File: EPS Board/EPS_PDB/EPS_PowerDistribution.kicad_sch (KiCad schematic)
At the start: 73 parts, among them U10 TPS259621DDAT, U11 LTC3624IDD-25PBF, U12 TPS259621DDAT, U13 TPS259621DDAT, U14 TPS259621DDAT, U15 TPS259621DDAT, U16 TPS259621DDAT, U17 LM5000-3MTCX, U18 AD7708BRUZ, U2 TS4061BICT-1.25, U6 TPS259621DDAT, U7 TPS259621DDAT, U9 TPS259621DDAT, Y4 32.768kHz

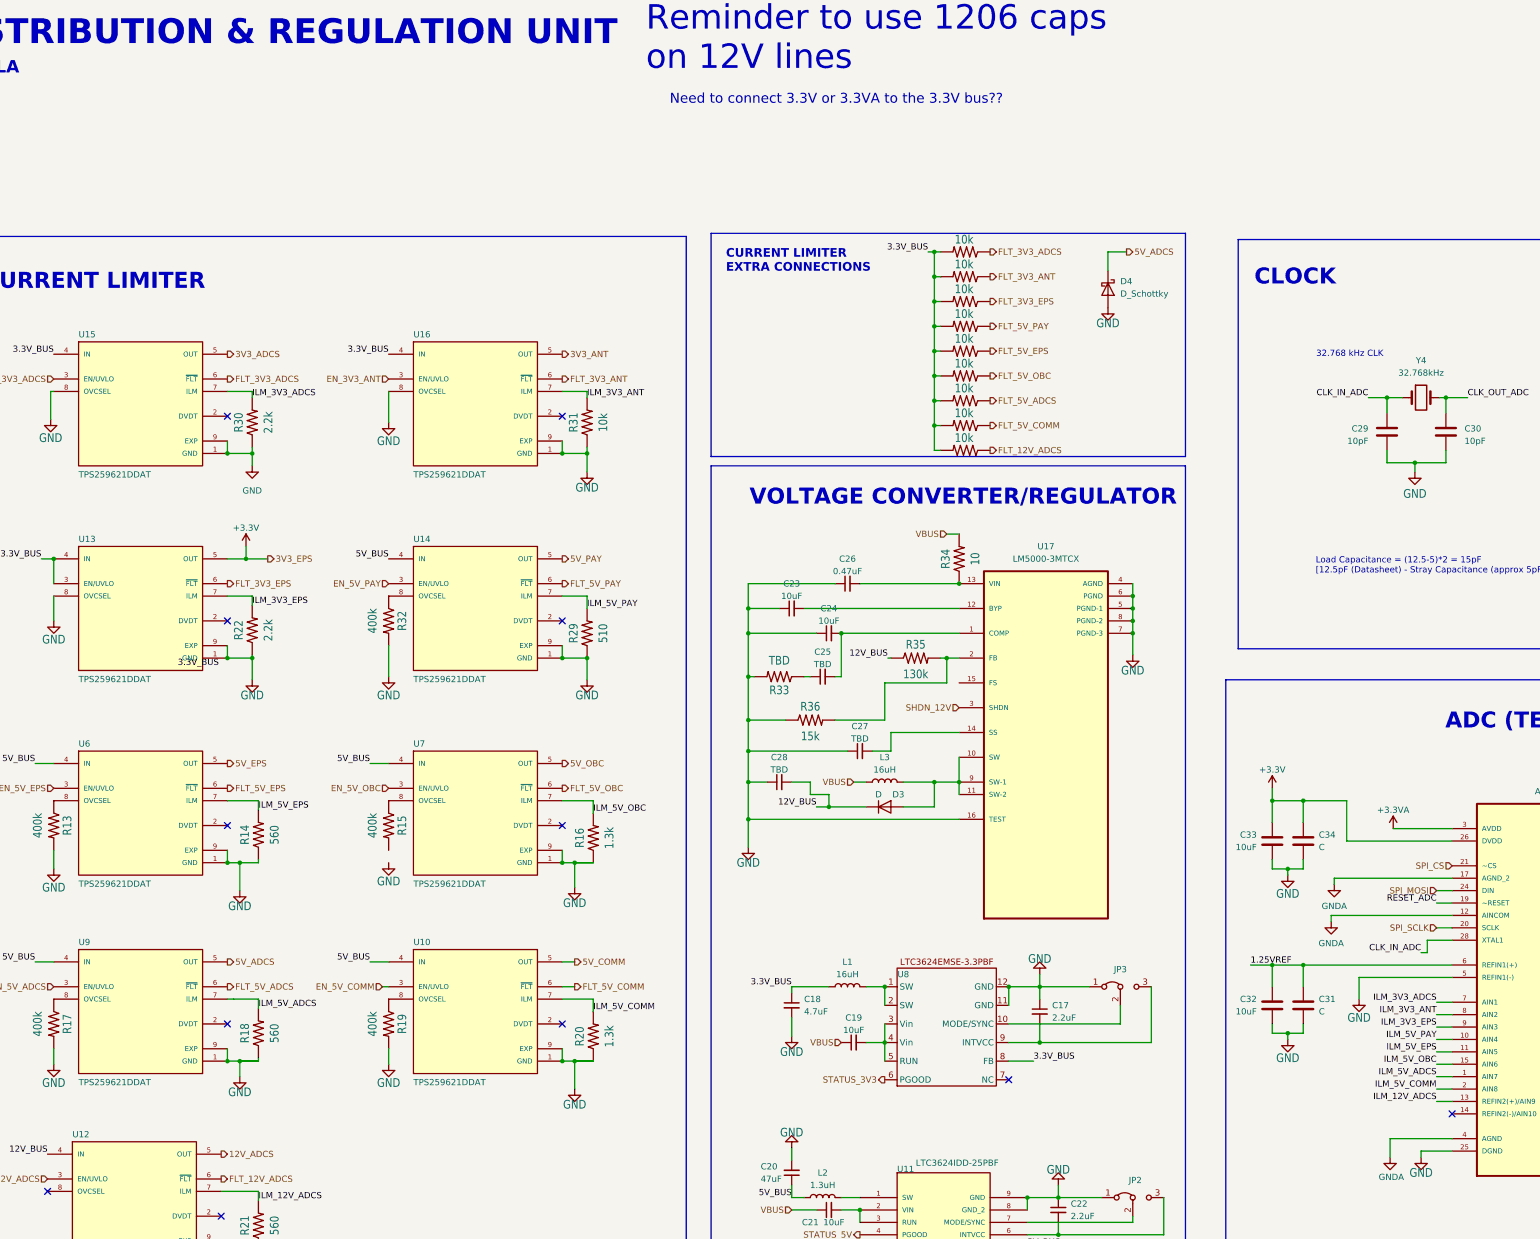
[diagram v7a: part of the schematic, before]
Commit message: texts added in schematics for clarity
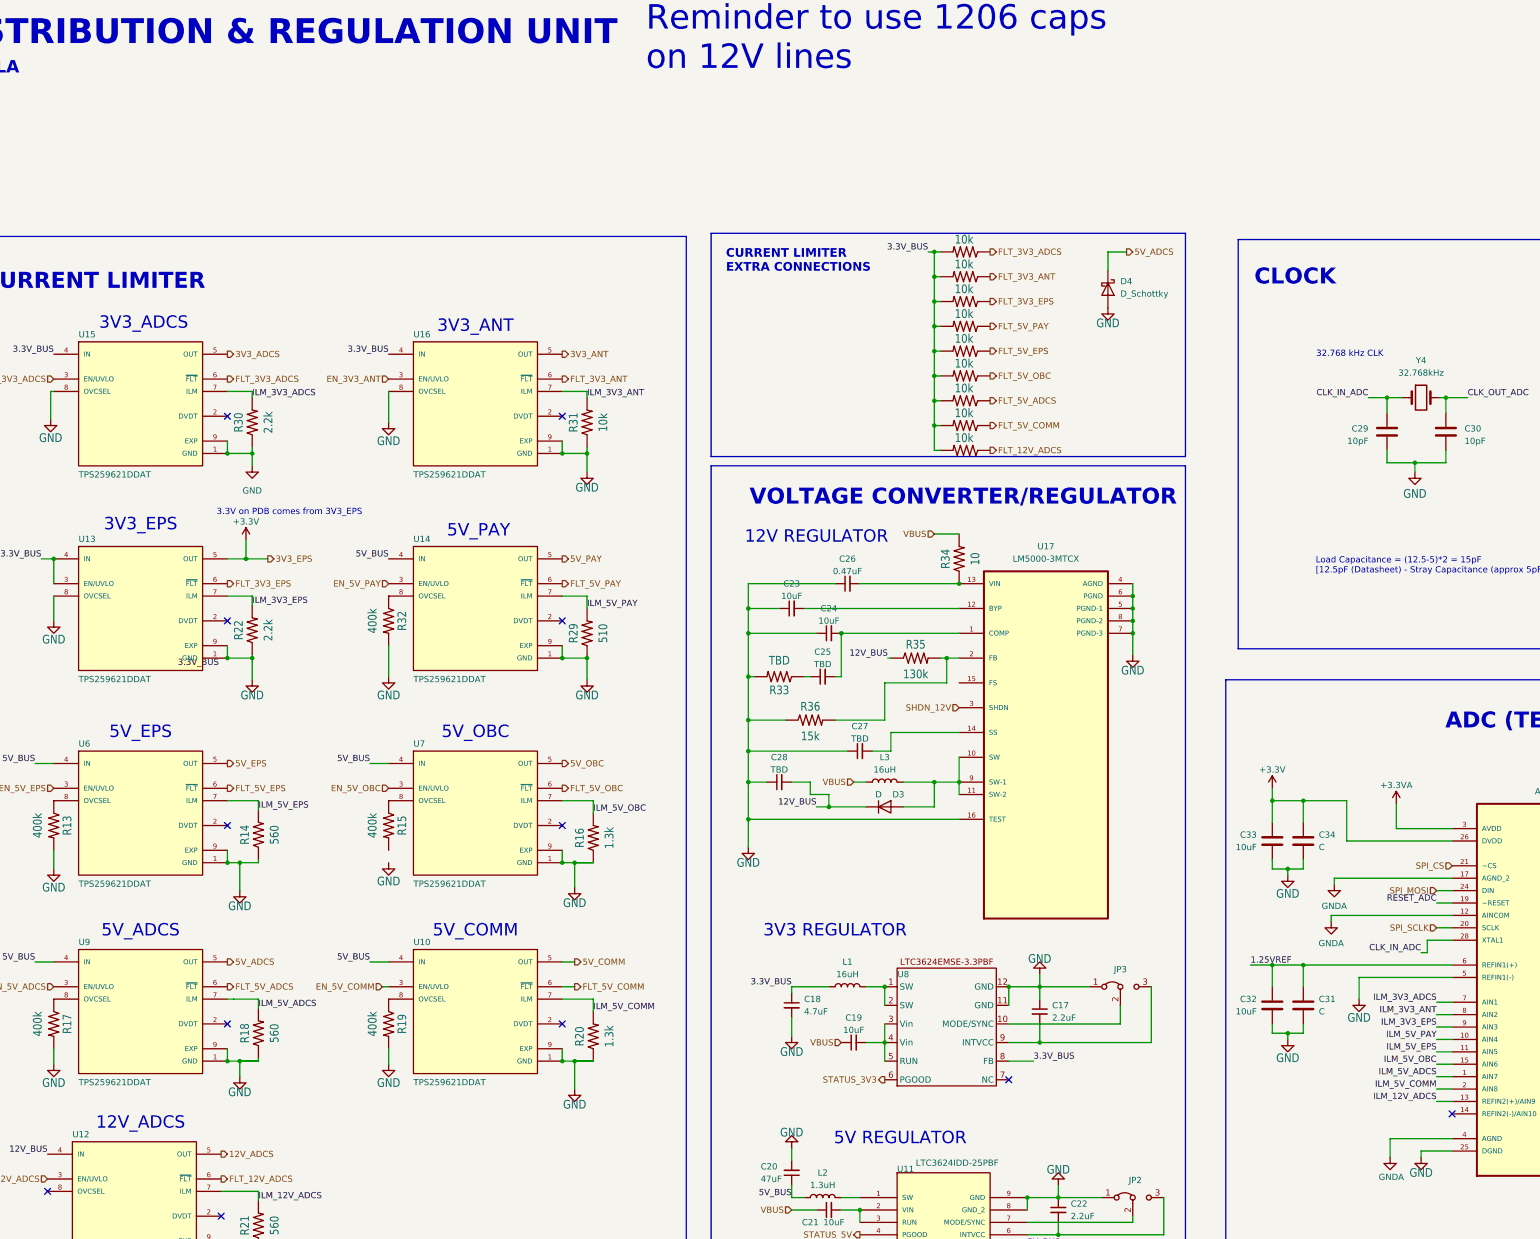
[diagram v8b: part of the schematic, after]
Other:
- note added: "12V REGULATOR"
- note added: "12V_ADCS"
- note added: "3.3V on PDB comes from 3V3_EPS"
- note added: "3V3 REGULATOR"
- note added: "3V3_ADCS"
- note added: "3V3_ANT"
- note added: "3V3_EPS"
- note added: "5V REGULATOR"
- note added: "5V_ADCS"
- note added: "5V_COMM"
- note added: "5V_EPS"
- note added: "5V_OBC"
- note added: "5V_PAY"
- note removed: "Need to connect 3.3V or 3.3VA to the 3.3V bus??"
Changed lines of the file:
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@@
 	(wire
 		(pts
-			(xy 334.01 186.69) (xy 346.075 186.69)
-		)
-		(stroke
-			(width 0)
-			(type default)
-		)
-	)
-	(wire
-		(pts
 			(xy 128.27 234.95) (xy 128.27 231.775)
 		)
@@
 	(wire
 		(pts
-			(xy 242.57 126.365) (xy 245.11 126.365)
+			(xy 240.03 126.365) (xy 245.11 126.365)
 		)
 		(stroke
@@
 	(wire
 		(pts
-			(xy 99.06 128.905) (xy 99.06 131.445)
+			(xy 99.06 127.635) (xy 99.06 131.445)
+		)
+		(stroke
+			(width 0)
+			(type default)
+		)
+	)
+	(wire
+		(pts
+			(xy 334.645 186.69) (xy 346.075 186.69)
 		)
 		(stroke
@@
 	(wire
 		(pts
+			(xy 334.645 181.61) (xy 334.645 186.69)
+		)
+		(stroke
+			(width 0)
+			(type default)
+		)
+	)
+	(wire
+		(pts
 			(xy 201.93 155.575) (xy 203.2 155.575)
 		)
@@
 		)
 	)
-	(text "Need to connect 3.3V or 3.3VA to the 3.3V bus??"
-		(exclude_from_sim no)
-		(at 219.964 37.338 0)
-		(effects
-			(font
-				(size 2.032 2.032)
-			)
-		)
-	)
 	(text "VOLTAGE CONVERTER/REGULATOR"
 		(exclude_from_sim no)
@@
 		)
 	)
+	(text "5V_EPS"
+		(exclude_from_sim no)
+		(at 77.47 167.005 0)
+		(effects
+			(font
+				(size 2.54 2.54)
+			)
+		)
+	)
 	(text "ADC (TELEMETRY)"
 		(exclude_from_sim no)
@@
 		)
 	)
+	(text "12V_ADCS"
+		(exclude_from_sim no)
+		(at 77.47 247.015 0)
+		(effects
+			(font
+				(size 2.54 2.54)
+			)
+		)
+	)
+	(text "5V_OBC"
+		(exclude_from_sim no)
+		(at 146.05 167.005 0)
+		(effects
+			(font
+				(size 2.54 2.54)
+			)
+		)
+	)
+	(text "12V REGULATOR"
+		(exclude_from_sim no)
+		(at 215.9 127 0)
+		(effects
+			(font
+				(size 2.54 2.54)
+			)
+		)
+	)
+	(text "5V_ADCS"
+		(exclude_from_sim no)
+		(at 77.47 207.645 0)
+		(effects
+			(font
+				(size 2.54 2.54)
+			)
+		)
+	)
+	(text "5V_COMM"
+		(exclude_from_sim no)
+		(at 146.05 207.645 0)
+		(effects
+			(font
+				(size 2.54 2.54)
+			)
+		)
+	)
+	(text "3V3_ANT"
+		(exclude_from_sim no)
+		(at 146.05 83.82 0)
+		(effects
+			(font
+				(size 2.54 2.54)
+			)
+		)
+	)
 	(text "CURRENT LIMITER \nEXTRA CONNECTIONS"
 		(exclude_from_sim no)
@@
 		)
 	)
+	(text "3.3V on PDB comes from 3V3_EPS"
+		(exclude_from_sim no)
+		(at 107.95 121.92 0)
+		(effects
+			(font
+				(size 1.27 1.27)
+			)
+		)
+	)
+	(text "3V3_EPS"
+		(exclude_from_sim no)
+		(at 77.47 124.46 0)
+		(effects
+			(font
+				(size 2.54 2.54)
+			)
+		)
+	)
+	(text "5V_PAY"
+		(exclude_from_sim no)
+		(at 146.685 125.73 0)
+		(effects
+			(font
+				(size 2.54 2.54)
+			)
+		)
+	)
 	(text "VDDA Filtering"
 		(exclude_from_sim no)
@@
 		)
 	)
+	(text "3V3 REGULATOR"
+		(exclude_from_sim no)
+		(at 219.71 207.645 0)
+		(effects
+			(font
+				(size 2.54 2.54)
+			)
+		)
+	)
 	(text "REF pin consumes 0.5uA current"
 		(exclude_from_sim no)
@@
 		)
 	)
+	(text "5V REGULATOR"
+		(exclude_from_sim no)
+		(at 233.045 250.19 0)
+		(effects
+			(font
+				(size 2.54 2.54)
+			)
+		)
+	)
+	(text "3V3_ADCS"
+		(exclude_from_sim no)
+		(at 78.105 83.185 0)
+		(effects
+			(font
+				(size 2.54 2.54)
+			)
+		)
+	)
 	(text "15mA > (3.3-1.25)/R > 10uA (min input current)\n136.67 Ohm < R < 205 kOhm"
 		(exclude_from_sim no)
@@
 	(hierarchical_label "VBUS"
 		(shape input)
-		(at 242.57 126.365 180)
+		(at 240.03 126.365 180)
 		(fields_autoplaced yes)
 		(effects
@@
 	(symbol
 		(lib_id "power:+3.3VA")
-		(at 334.01 186.69 0)
+		(at 334.645 181.61 0)
 		(unit 1)
 		(exclude_from_sim no)
@@
 		(on_board yes)
 		(dnp no)
-		(fields_autoplaced yes)
 		(property "Reference" "#PWR048"
-			(at 334.01 190.5 0)
+			(at 334.645 185.42 0)
 			(effects
 				(font
@@
 		)
 		(property "Value" "+3.3VA"
-			(at 334.01 182.88 0)
+			(at 334.645 177.8 0)
 			(effects
 				(font
@@
 		)
 		(property "Footprint" ""
-			(at 334.01 186.69 0)
+			(at 334.645 181.61 0)
 			(effects
 				(font
@@
 		)
 		(property "Datasheet" ""
-			(at 334.01 186.69 0)
+			(at 334.645 181.61 0)
 			(effects
 				(font
@@
 		)
 		(property "Description" ""
-			(at 334.01 186.69 0)
+			(at 334.645 181.61 0)
 			(effects
 				(font
@@
 	(symbol
 		(lib_id "power:+3.3V")
-		(at 99.06 128.905 0)
+		(at 99.06 127.635 0)
 		(unit 1)
 		(exclude_from_sim no)
@@
 		(fields_autoplaced yes)
 		(property "Reference" "#PWR051"
-			(at 99.06 132.715 0)
+			(at 99.06 131.445 0)
 			(effects
 				(font
@@
 		)
 		(property "Value" "+3.3V"
-			(at 99.06 125.095 0)
+			(at 99.06 123.825 0)
 			(effects
 				(font
@@
 		)
 		(property "Footprint" ""
-			(at 99.06 128.905 0)
+			(at 99.06 127.635 0)
 			(effects
 				(font
@@
 		)
 		(property "Datasheet" ""
-			(at 99.06 128.905 0)
+			(at 99.06 127.635 0)
 			(effects
 				(font
@@
 		)
 		(property "Description" ""
-			(at 99.06 128.905 0)
+			(at 99.06 127.635 0)
 			(effects
 				(font
